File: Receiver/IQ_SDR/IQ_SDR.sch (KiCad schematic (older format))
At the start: 97 parts, among them CON1 SJ1-3523N, J1 ANT, J10 LO_I, J11 LO_Q, J12 GNDA, J13 I_IN, J14 Q_IN, J15 +5V, J16 4.3V, J17 I_OUT, J18 Q_OUT, J19 Conn_01x01_Male, J2 GND, J20 Conn_01x01_Male, J3 V_IN pin header, J4 GND, J5 V_IN, J6 FIL_O, J7 CLK1, J8 CLK2, J9 CLK0, P1 BNC, P2 SMA, Q1 MMBT2222A-TP, T1 Transformer_1P_SS, U1 FST3253, U2 Si5351A-B-GT, U3 TS5A23157, U4 LM4562 or LT6231, U5 74ALVC74D, Y1 CX3225

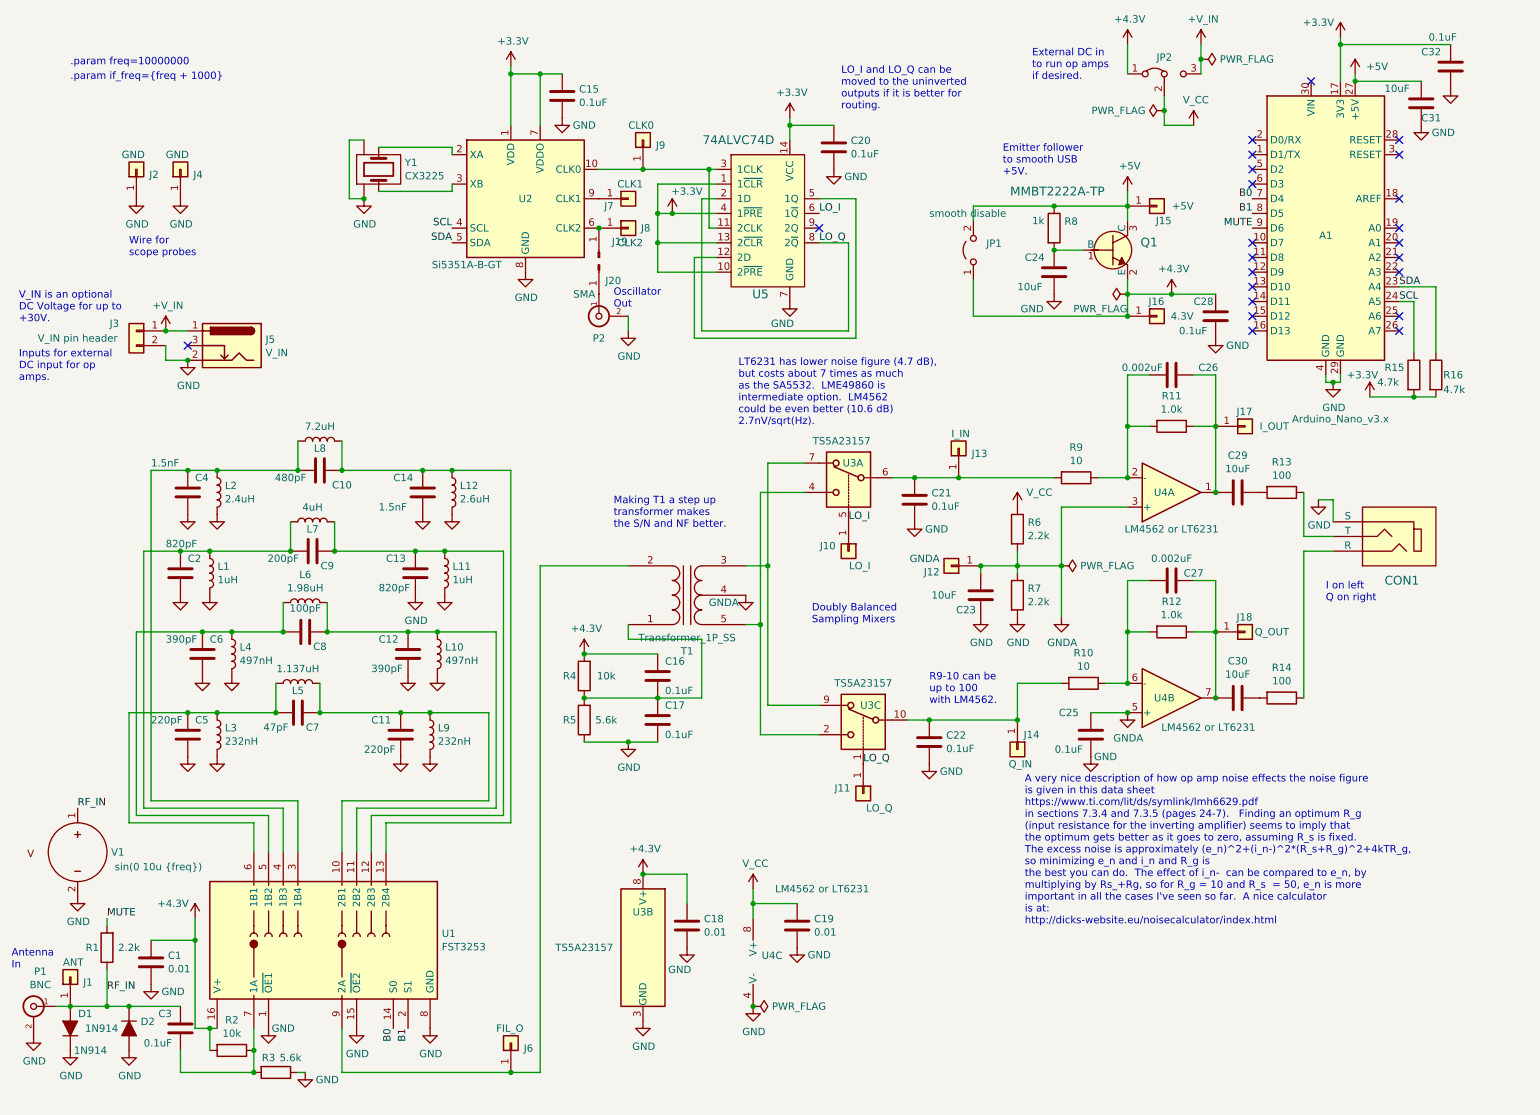
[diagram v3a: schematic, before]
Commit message: Add inductor/transformer details.  Change U1 package type.  (Maybe should change the IC as we did in rev 0.1.)
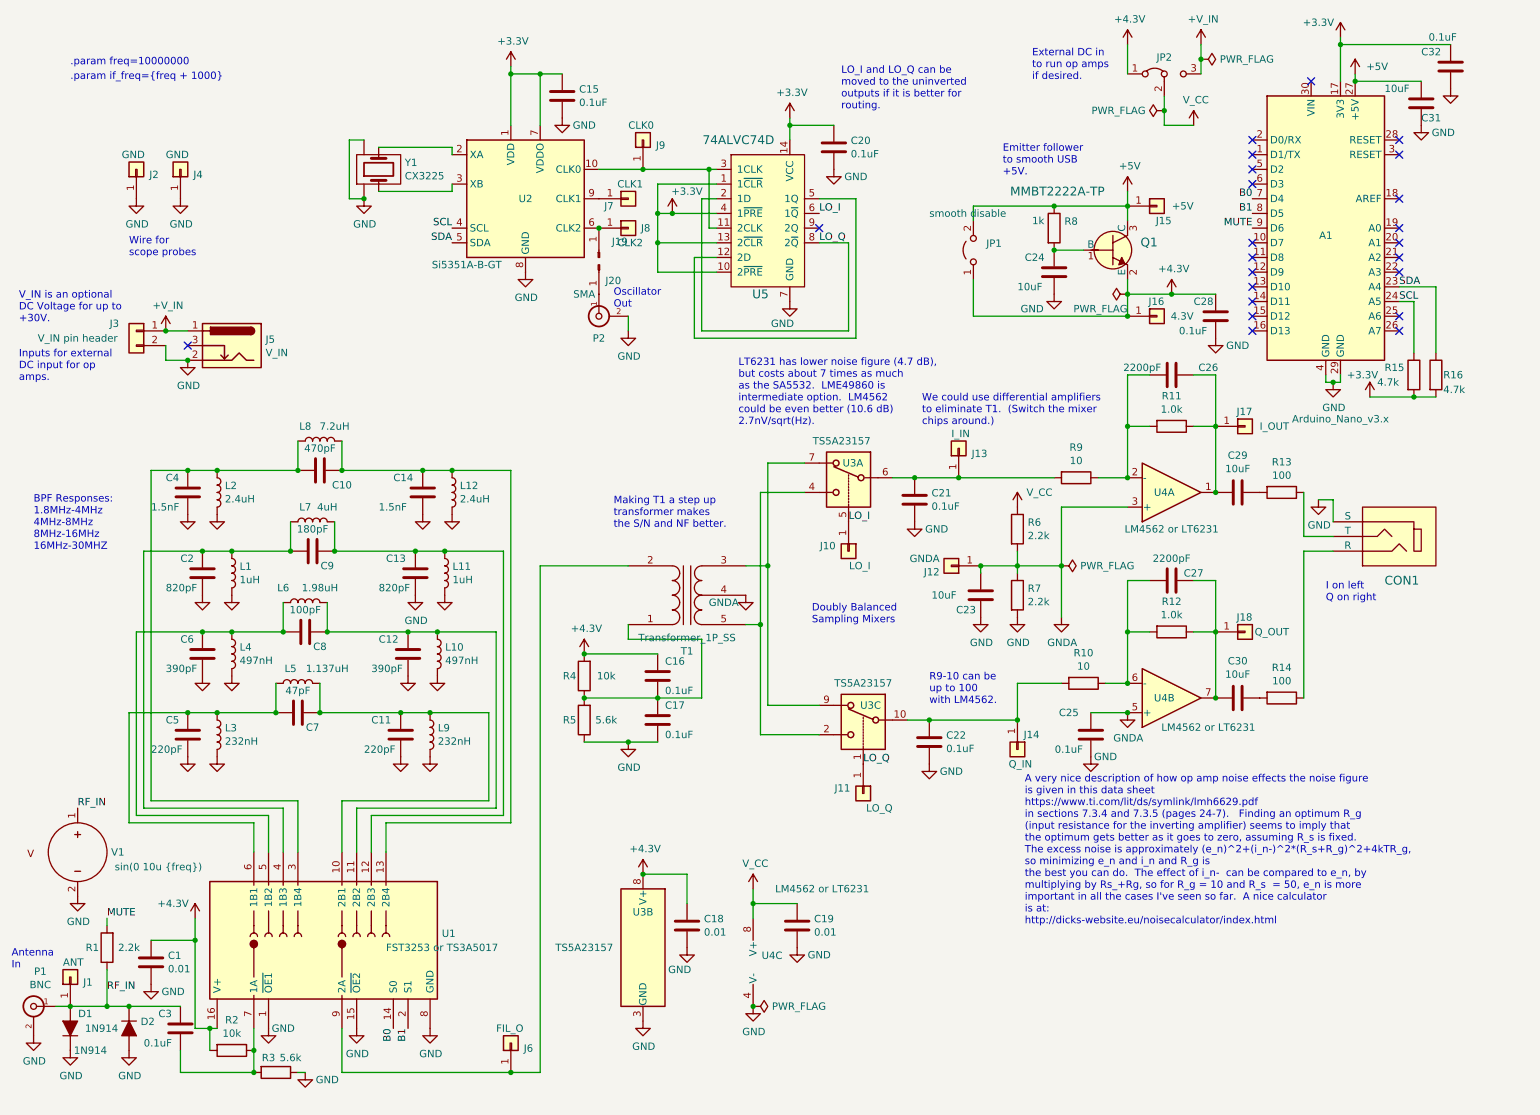
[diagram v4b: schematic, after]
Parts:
- C10: value 480pF -> 470pF
- C26, C27: value 0.002uF -> 2200pF
- C9: value 200pF -> 180pF
- L1, L11: Winding (none) -> T37-6, #30 wire, 18 turns
- L12: value 2.6uH -> 2.4uH; Winding (none) -> T50-6, #30 wire, 25 turns
- L2: Winding (none) -> T50-6, #30 wire, 25 turns
- L3, L9: Winding (none) -> T37-6, #30 wire, 9 turns
- L5: Winding (none) -> T37-6, #30 wire, 20 turns
- L6: Winding (none) -> T37-6, #30 wire, 26 turns
- L7: Winding (none) -> T50-6, #30 wire, 32 turns
- L8: Winding (none) -> T50-6 #30 wire, 43 turns
- T1: Winding (none) -> BN-43-2402, #30, primary 5\", seconday 2x3\" bifilar
- U1: value FST3253 -> FST3253 or TS3A5017; footprint Housings_SOIC:SOIC-16_3.9x9.9mm_Pitch1.27mm -> Housings_SSOP:TSSOP-16_4.4x5mm_Pitch0.65mm
- U4: footprint SMA:DMP8 -> Housings_SOIC:SOIC-8_3.9x4.9mm_Pitch1.27mm
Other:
- note added: "BPF Responses:\n1.8MHz-4MHz\n4MHz-8MHz\n8MHz-16MHz\n16MHz-30MHZ"
- note added: "We could use differential amplifiers\nto eliminate T1. (Switch the mixer\nchips around.)"
- moved on the sheet: C2, L1
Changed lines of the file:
@@
 EESchema Schematic File Version 4
 LIBS:IQ_SDR-cache
-EELAYER 29 0
+EELAYER 30 0
 EELAYER END
 $Descr USLetter 11000 8500
@@
 F 0 "U4" H 8450 5150 50  0000 C CNN
 F 1 "LM4562 or LT6231" H 8750 5350 50  0000 C CNN
-F 2 "SMA:DMP8" H 8500 5150 50  0001 C CNN
+F 2 "Housings_SOIC:SOIC-8_3.9x4.9mm_Pitch1.27mm" H 8500 5150 50  0001 C CNN
 F 3 "https://www.analog.com/media/en/technical-documentation/data-sheets/623012fc.pdf" H 8500 5150 50  0001 C CNN
 F 4 "X" H 8500 5150 50  0001 C CNN "Spice_Primitive"
@@
 P 8500 4350
 F 0 "C27" V 8450 4500 50  0000 C CNN
-F 1 "0.002uF" V 8350 4350 50  0000 C CNN
+F 1 "2200pF" V 8350 4350 50  0000 C CNN
 F 2 "Capacitors_SMD:C_0805" H 8538 4200 50  0001 C CNN
 F 3 "~" H 8500 4350 50  0001 C CNN
@@
 P 8500 2950
 F 0 "C26" V 8450 3200 50  0000 C CNN
-F 1 "0.002uF" V 8450 2750 50  0000 C CNN
+F 1 "2200pF" V 8450 2750 50  0000 C CNN
 F 2 "Capacitors_SMD:C_0805" H 8538 2800 50  0001 C CNN
 F 3 "~" H 8500 2950 50  0001 C CNN
@@
 P 2700 6800
 F 0 "U1" V 2746 5970 50  0000 R CNN
-F 1 "FST3253" V 2655 5970 50  0000 R CNN
-F 2 "Housings_SOIC:SOIC-16_3.9x9.9mm_Pitch1.27mm" H 2700 5900 50  0001 C CNN
+F 1 "FST3253 or TS3A5017 " V 2650 6350 50  0000 R CNN
+F 2 "Housings_SSOP:TSSOP-16_4.4x5mm_Pitch0.65mm" H 2700 5900 50  0001 C CNN
 F 3 "https://www.onsemi.com/pub/Collateral/FST3253-D.pdf" H 2700 5700 50  0001 C CNN
 F 4 "DIST DIGIKEY FST3253MXFSCT-ND" H 2700 5800 60  0001 C CNN "BOM"
@@
 F 2 "SMA:4_to_1_Transmission_Line_TransformerTHT" H 5200 4450 50  0001 C CNN
 F 3 "~" H 5200 4450 50  0001 C CNN
+F 4 "BN-43-2402, #30, primary 5\", seconday 2x3\" bifilar" H 5200 4450 50  0001 C CNN "Winding"
 	1    5200 4450
 	1    0    0    1
@@
 U 1 1 5D17E138
 P 2700 3400
-F 0 "L8" V 2650 3400 50  0000 C CNN
-F 1 "7.2uH" V 2799 3400 50  0000 C CNN
+F 0 "L8" V 2800 3500 50  0000 C CNN
+F 1 "7.2uH" V 2800 3300 50  0000 C CNN
 F 2 "Inductors_THT:L_Toroid_Vertical_L10.0mm_W5.0mm_P5.08mm" H 2700 3400 50  0001 C CNN
 F 3 "http://www.lodestonepacific.com/distrib/pdfs/Micrometals/RFA_Cat.pdf" H 2700 3400 50  0001 C CNN
+F 4 "T50-6 #30 wire, 43 turns" V 2700 3400 50  0001 C CNN "Winding"
 	1    2700 3400
 	0    -1   -1   0
@@
 P 2700 3600
 F 0 "C10" V 2800 3750 50  0000 C CNN
-F 1 "480pF" V 2750 3400 50  0000 C CNN
+F 1 "470pF" V 2550 3600 50  0000 C CNN
 F 2 "Capacitors_SMD:C_0805" H 2738 3450 50  0001 C CNN
 F 3 "~" H 2700 3600 50  0001 C CNN
@@
 U 1 1 5D17EABA
 P 1800 3750
-F 0 "C4" H 1850 3850 50  0000 L CNN
-F 1 "1.5nF" H 1550 3950 50  0000 L CNN
+F 0 "C4" H 1650 3850 50  0000 L CNN
+F 1 "1.5nF" H 1550 3650 50  0000 L CNN
 F 2 "Capacitors_SMD:C_0805" H 1838 3600 50  0001 C CNN
 F 3 "~" H 1800 3750 50  0001 C CNN
@@
 F 2 "Inductors_THT:L_Toroid_Vertical_L10.0mm_W5.0mm_P5.08mm" H 2000 3750 50  0001 C CNN
 F 3 "http://www.lodestonepacific.com/distrib/pdfs/Micrometals/RFA_Cat.pdf" H 2000 3750 50  0001 C CNN
+F 4 "T50-6, #30 wire, 25 turns" H 2000 3750 50  0001 C CNN "Winding"
 	1    2000 3750
 	1    0    0    -1
@@
 P 3600 3750
 F 0 "L12" H 3653 3796 50  0000 L CNN
-F 1 "2.6uH" H 3653 3705 50  0000 L CNN
+F 1 "2.4uH" H 3653 3705 50  0000 L CNN
 F 2 "Inductors_THT:L_Toroid_Vertical_L10.0mm_W5.0mm_P5.08mm" H 3600 3750 50  0001 C CNN
 F 3 "http://www.lodestonepacific.com/distrib/pdfs/Micrometals/RFA_Cat.pdf" H 3600 3750 50  0001 C CNN
+F 4 "T50-6, #30 wire, 25 turns" H 3600 3750 50  0001 C CNN "Winding"
 	1    3600 3750
 	1    0    0    -1
@@
 U 1 1 5D1D3FF4
 P 2650 3950
-F 0 "L7" V 2600 3950 50  0000 C CNN
-F 1 "4uH" V 2749 3950 50  0000 C CNN
+F 0 "L7" V 2750 4000 50  0000 C CNN
+F 1 "4uH" V 2750 3850 50  0000 C CNN
 F 2 "Inductors_THT:L_Toroid_Vertical_L10.0mm_W5.0mm_P5.08mm" H 2650 3950 50  0001 C CNN
 F 3 "http://www.lodestonepacific.com/distrib/pdfs/Micrometals/RFA_Cat.pdf" H 2650 3950 50  0001 C CNN
+F 4 "T50-6, #30 wire, 32 turns" V 2650 3950 50  0001 C CNN "Winding"
 	1    2650 3950
 	0    -1   -1   0
@@
 P 2650 4150
 F 0 "C9" V 2750 4250 50  0000 C CNN
-F 1 "200pF" V 2700 3950 50  0000 C CNN
+F 1 "180pF" V 2500 4150 50  0000 C CNN
 F 2 "Capacitors_SMD:C_0805" H 2688 4000 50  0001 C CNN
 F 3 "~" H 2650 4150 50  0001 C CNN
@@
 L Device:C C2
 U 1 1 5D1D4002
-P 1750 4300
-F 0 "C2" H 1800 4400 50  0000 L CNN
-F 1 "820pF" H 1650 4500 50  0000 L CNN
-F 2 "Capacitors_SMD:C_0805" H 1788 4150 50  0001 C CNN
-F 3 "~" H 1750 4300 50  0001 C CNN
-	1    1750 4300
+P 1900 4300
+F 0 "C2" H 1750 4400 50  0000 L CNN
+F 1 "820pF" H 1650 4200 50  0000 L CNN
+F 2 "Capacitors_SMD:C_0805" H 1938 4150 50  0001 C CNN
+F 3 "~" H 1900 4300 50  0001 C CNN
+	1    1900 4300
 	1    0    0    -1
 $EndComp
@@
 L Device:L L1
 U 1 1 5D1D4009
-P 1950 4300
-F 0 "L1" H 2003 4346 50  0000 L CNN
-F 1 "1uH" H 2003 4255 50  0000 L CNN
-F 2 "Inductors_THT:L_Toroid_Vertical_L10.0mm_W5.0mm_P5.08mm" H 1950 4300 50  0001 C CNN
-F 3 "http://www.lodestonepacific.com/distrib/pdfs/Micrometals/RFA_Cat.pdf" H 1950 4300 50  0001 C CNN
-	1    1950 4300
+P 2100 4300
+F 0 "L1" H 2153 4346 50  0000 L CNN
+F 1 "1uH" H 2153 4255 50  0000 L CNN
+F 2 "Inductors_THT:L_Toroid_Vertical_L10.0mm_W5.0mm_P5.08mm" H 2100 4300 50  0001 C CNN
+F 3 "http://www.lodestonepacific.com/distrib/pdfs/Micrometals/RFA_Cat.pdf" H 2100 4300 50  0001 C CNN
+F 4 "T37-6, #30 wire, 18 turns" H 2100 4300 50  0001 C CNN "Winding"
+	1    2100 4300
 	1    0    0    -1
 $EndComp
@@
 F 2 "Inductors_THT:L_Toroid_Vertical_L10.0mm_W5.0mm_P5.08mm" H 3550 4300 50  0001 C CNN
 F 3 "http://www.lodestonepacific.com/distrib/pdfs/Micrometals/RFA_Cat.pdf" H 3550 4300 50  0001 C CNN
+F 4 "T37-6, #30 wire, 18 turns" H 3550 4300 50  0001 C CNN "Winding"
 	1    3550 4300
 	1    0    0    -1
@@
 L power:GND #PWR09
 U 1 1 5D1D401E
-P 1750 4450
-F 0 "#PWR09" H 1750 4200 50  0001 C CNN
-F 1 "GND" H 1755 4277 50  0001 C CNN
-F 2 "" H 1750 4450 50  0001 C CNN
-F 3 "" H 1750 4450 50  0001 C CNN
-	1    1750 4450
+P 1900 4450
+F 0 "#PWR09" H 1900 4200 50  0001 C CNN
+F 1 "GND" H 1905 4277 50  0001 C CNN
+F 2 "" H 1900 4450 50  0001 C CNN
+F 3 "" H 1900 4450 50  0001 C CNN
+	1    1900 4450
 	1    0    0    -1
 $EndComp
@@
 L power:GND #PWR015
 U 1 1 5D1D4024
-P 1950 4450
-F 0 "#PWR015" H 1950 4200 50  0001 C CNN
-F 1 "GND" H 1955 4277 50  0001 C CNN
-F 2 "" H 1950 4450 50  0001 C CNN
-F 3 "" H 1950 4450 50  0001 C CNN
-	1    1950 4450
+P 2100 4450
+F 0 "#PWR015" H 2100 4200 50  0001 C CNN
+F 1 "GND" H 2105 4277 50  0001 C CNN
+F 2 "" H 2100 4450 50  0001 C CNN
+F 3 "" H 2100 4450 50  0001 C CNN
+	1    2100 4450
 	1    0    0    -1
 $EndComp
@@
 $EndComp
 Wire Wire Line
-	1500 4150 1750 4150
-Connection ~ 1750 4150
-Wire Wire Line
-	1750 4150 1950 4150
-Connection ~ 1950 4150
-Wire Wire Line
-	1950 4150 2500 4150
+	1500 4150 1900 4150
+Connection ~ 1900 4150
+Wire Wire Line
+	1900 4150 2100 4150
+Connection ~ 2100 4150
+Wire Wire Line
+	2100 4150 2500 4150
 Wire Wire Line
 	2800 4150 3350 4150
@@
 U 1 1 5D22E31C
 P 2600 4500
-F 0 "L6" V 2790 4500 50  0000 C CNN
-F 1 "1.98uH" V 2699 4500 50  0000 C CNN
+F 0 "L6" V 2700 4650 50  0000 C CNN
+F 1 "1.98uH" V 2700 4400 50  0000 C CNN
 F 2 "Inductors_THT:L_Toroid_Vertical_L10.0mm_W5.0mm_P5.08mm" H 2600 4500 50  0001 C CNN
 F 3 "http://www.lodestonepacific.com/distrib/pdfs/Micrometals/RFA_Cat.pdf" H 2600 4500 50  0001 C CNN
+F 4 "T37-6, #30 wire, 26 turns" V 2600 4500 50  0001 C CNN "Winding"
 	1    2600 4500
 	0    -1   -1   0
@@
 P 2600 4700
 F 0 "C8" V 2700 4800 50  0000 C CNN
-F 1 "100pF" V 2439 4700 50  0000 C CNN
+F 1 "100pF" V 2450 4700 50  0000 C CNN
 F 2 "Capacitors_SMD:C_0805" H 2638 4550 50  0001 C CNN
 F 3 "~" H 2600 4700 50  0001 C CNN
@@
 U 1 1 5D22E32A
 P 1900 4850
-F 0 "C6" H 1950 4950 50  0000 L CNN
-F 1 "390pF" H 1650 4950 50  0000 L CNN
+F 0 "C6" H 1750 4950 50  0000 L CNN
+F 1 "390pF" H 1650 4750 50  0000 L CNN
 F 2 "Capacitors_SMD:C_0805" H 1938 4700 50  0001 C CNN
 F 3 "~" H 1900 4850 50  0001 C CNN
@@
 U 1 1 5D258FC6
 P 2550 5050
-F 0 "L5" V 2500 5050 50  0000 C CNN
-F 1 "1.137uH" V 2649 5050 50  0000 C CNN
+F 0 "L5" V 2650 5100 50  0000 C CNN
+F 1 "1.137uH" V 2650 4850 50  0000 C CNN
 F 2 "Inductors_THT:L_Toroid_Vertical_L10.0mm_W5.0mm_P5.08mm" H 2550 5050 50  0001 C CNN
 F 3 "http://www.lodestonepacific.com/distrib/pdfs/Micrometals/RFA_Cat.pdf" H 2550 5050 50  0001 C CNN
+F 4 "T37-6, #30 wire, 20 turns" V 2550 5050 50  0001 C CNN "Winding"
 	1    2550 5050
 	0    -1   -1   0
@@
 P 2550 5250
 F 0 "C7" V 2650 5350 50  0000 C CNN
-F 1 "47pF" V 2650 5100 50  0000 C CNN
+F 1 "47pF" V 2400 5250 50  0000 C CNN
 F 2 "Capacitors_SMD:C_0805" H 2588 5100 50  0001 C CNN
 F 3 "~" H 2550 5250 50  0001 C CNN
@@
 U 1 1 5D258FD4
 P 1800 5400
-F 0 "C5" H 1850 5500 50  0000 L CNN
-F 1 "220pF" H 1550 5500 50  0000 L CNN
+F 0 "C5" H 1650 5500 50  0000 L CNN
+F 1 "220pF" H 1550 5300 50  0000 L CNN
 F 2 "Capacitors_SMD:C_0805" H 1838 5250 50  0001 C CNN
 F 3 "~" H 1800 5400 50  0001 C CNN
@@
 F 2 "Inductors_THT:L_Toroid_Vertical_L10.0mm_W5.0mm_P5.08mm" H 2000 5400 50  0001 C CNN
 F 3 "http://www.lodestonepacific.com/distrib/pdfs/Micrometals/RFA_Cat.pdf" H 2000 5400 50  0001 C CNN
+F 4 "T37-6, #30 wire, 9 turns" H 2000 5400 50  0001 C CNN "Winding"
 	1    2000 5400
 	1    0    0    -1
@@
 F 2 "Inductors_THT:L_Toroid_Vertical_L10.0mm_W5.0mm_P5.08mm" H 3450 5400 50  0001 C CNN
 F 3 "http://www.lodestonepacific.com/distrib/pdfs/Micrometals/RFA_Cat.pdf" H 3450 5400 50  0001 C CNN
+F 4 "T37-6, #30 wire, 9 turns" H 3450 5400 50  0001 C CNN "Winding"
 	1    3450 5400
 	1    0    0    -1
@@
 	10150 3100 10300 3100
 Connection ~ 10150 3100
+Text Notes 750  4150 0    50   ~ 0
+BPF Responses:\n1.8MHz-4MHz\n4MHz-8MHz\n8MHz-16MHz\n16MHz-30MHZ
+Text Notes 6800 3300 0    50   ~ 0
+We could use differential amplifiers\nto eliminate T1.  (Switch the mixer\nchips around.)
 $EndSCHEMATC

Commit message: saving changes so I can merge from hamshack.
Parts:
- A1: symbol MCU_Module:Arduino_Nano_v3.x -> IQ_SDR-rescue:Arduino_Nano_v3.x-MCU_Module
- C1, C10, C11, C12, C13, C14, C15, C16, C17, C18, C19, C2, C20, C21, C22, C23, C24, C25, C26, C27, C28, C29, C3, C30, C31, C32, C4, C5, C6, C7, C8, C9: symbol Device:C -> IQ_SDR-rescue:C-Device
- D1, D2: symbol Device:D_ALT -> IQ_SDR-rescue:D_ALT-Device
- J1, J10, J11, J12, J13, J14, J15, J16, J17, J18, J2, J4, J6, J7, J8, J9: symbol Connector_Generic:Conn_01x01 -> IQ_SDR-rescue:Conn_01x01-Connector_Generic
- J3: symbol Connector_Generic:Conn_01x02 -> IQ_SDR-rescue:Conn_01x02-Connector_Generic
- JP1: symbol Jumper:Jumper_2_Open -> IQ_SDR-rescue:Jumper_2_Open-Jumper
- JP2: symbol Jumper:Jumper_3_Bridged12 -> IQ_SDR-rescue:Jumper_3_Bridged12-Jumper
- L1, L10, L11, L12, L2, L3, L4, L5, L6, L7, L8, L9: symbol Device:L -> IQ_SDR-rescue:L-Device
- R1, R10, R11, R12, R13, R14, R15, R16, R2, R3, R4, R5, R6, R7, R8, R9: symbol Device:R -> IQ_SDR-rescue:R-Device
- T1: symbol Device:Transformer_1P_SS -> IQ_SDR-rescue:Transformer_1P_SS-Device
- U2: symbol Oscillator:Si5351A-B-GT -> IQ_SDR-rescue:Si5351A-B-GT-Oscillator
- U4: symbol Amplifier_Operational:NJM5532 -> IQ_SDR-rescue:NJM5532-Amplifier_Operational
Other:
- note added: "MASWSS0136 might\nbe better for mixers."
- note added: "Maybe change these diodes to LEDs."
- note added: "PO3B14A might\nbe better for\nTayloe mixer."
- note added: "PO74G74A would \nbe faster for the divider."
